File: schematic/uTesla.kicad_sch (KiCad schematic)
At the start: 0 parts

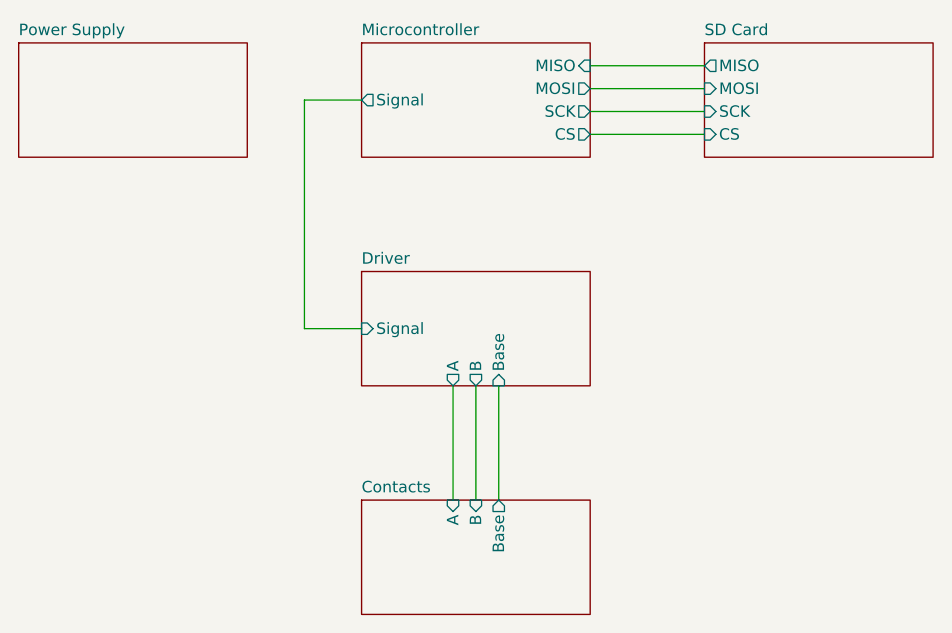
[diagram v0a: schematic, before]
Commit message: Create SD card schematic
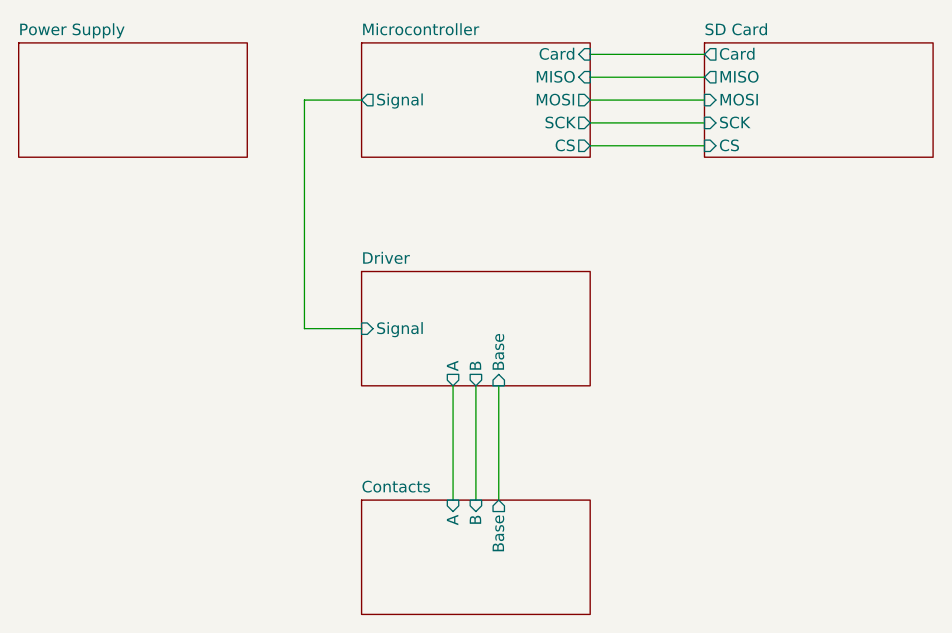
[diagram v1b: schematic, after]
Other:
- sheet Microcontroller ports: added Card; removed none
- sheet SD Card ports: added Card; removed none
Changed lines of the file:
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@@
 (kicad_sch (version 20230121) (generator eeschema)
   (paper "A4")
-  (wire (pts (xy 152.4 71.12) (xy 165.1 71.12))
-    (stroke (width 0) (type default))
-  )
   (wire (pts (xy 139.7 101.6) (xy 139.7 114.3))
     (stroke (width 0) (type default))
   )
-  (wire (pts (xy 152.4 73.66) (xy 165.1 73.66))
-    (stroke (width 0) (type default))
-  )
-  (wire (pts (xy 152.4 68.58) (xy 165.1 68.58))
-    (stroke (width 0) (type default))
-  )
-  (wire (pts (xy 152.4 66.04) (xy 165.1 66.04))
+  (wire (pts (xy 152.4 67.31) (xy 165.1 67.31))
     (stroke (width 0) (type default))
   )
@@
   )
   (wire (pts (xy 127 69.85) (xy 120.65 69.85))
+    (stroke (width 0) (type default))
+  )
+  (wire (pts (xy 152.4 64.77) (xy 165.1 64.77))
     (stroke (width 0) (type default))
   )
@@
   )
   (wire (pts (xy 142.24 101.6) (xy 142.24 114.3))
+    (stroke (width 0) (type default))
+  )
+  (wire (pts (xy 152.4 72.39) (xy 165.1 72.39))
+    (stroke (width 0) (type default))
+  )
+  (wire (pts (xy 152.4 74.93) (xy 165.1 74.93))
+    (stroke (width 0) (type default))
+  )
+  (wire (pts (xy 152.4 69.85) (xy 165.1 69.85))
     (stroke (width 0) (type default))
   )
@@
     (instances
       (project "uTesla"
-        (path "/0cecab2b-a552-4f9c-b012-66fc2b7d8bdb" (page "4"))
+        (path "/0cecab2b-a552-4f9c-b012-66fc2b7d8bdb" (page "5"))
       )
     )
@@
       (effects (font (size 1.27 1.27)) (justify left top) hide)
     )
-    (pin "MISO" output (at 165.1 66.04 180)
+    (pin "MISO" output (at 165.1 67.31 180)
       (effects (font (size 1.27 1.27)) (justify left))
     )
-    (pin "SCK" input (at 165.1 71.12 180)
+    (pin "SCK" input (at 165.1 72.39 180)
       (effects (font (size 1.27 1.27)) (justify left))
     )
-    (pin "CS" input (at 165.1 73.66 180)
+    (pin "CS" input (at 165.1 74.93 180)
       (effects (font (size 1.27 1.27)) (justify left))
     )
-    (pin "MOSI" input (at 165.1 68.58 180)
+    (pin "MOSI" input (at 165.1 69.85 180)
+      (effects (font (size 1.27 1.27)) (justify left))
+    )
+    (pin "Card" output (at 165.1 64.77 180)
       (effects (font (size 1.27 1.27)) (justify left))
     )
     (instances
       (project "uTesla"
-        (path "/0cecab2b-a552-4f9c-b012-66fc2b7d8bdb" (page "5"))
+        (path "/0cecab2b-a552-4f9c-b012-66fc2b7d8bdb" (page "4"))
       )
     )
@@
       (effects (font (size 1.27 1.27)) (justify left))
     )
-    (pin "MOSI" output (at 152.4 68.58 0)
+    (pin "MOSI" output (at 152.4 69.85 0)
       (effects (font (size 1.27 1.27)) (justify right))
     )
-    (pin "CS" output (at 152.4 73.66 0)
+    (pin "CS" output (at 152.4 74.93 0)
       (effects (font (size 1.27 1.27)) (justify right))
     )
-    (pin "MISO" input (at 152.4 66.04 0)
+    (pin "MISO" input (at 152.4 67.31 0)
       (effects (font (size 1.27 1.27)) (justify right))
     )
-    (pin "SCK" output (at 152.4 71.12 0)
+    (pin "SCK" output (at 152.4 72.39 0)
       (effects (font (size 1.27 1.27)) (justify right))
     )
+    (pin "Card" input (at 152.4 64.77 0)
+      (effects (font (size 1.27 1.27)) (justify right))
+    )

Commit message: Create driver schematic
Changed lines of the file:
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@@
       (effects (font (size 1.27 1.27)) (justify left top) hide)
     )
-    (pin "A" input (at 137.16 114.3 90)
+    (pin "Base" output (at 142.24 114.3 90)
       (effects (font (size 1.27 1.27)) (justify right))
     )
-    (pin "B" input (at 139.7 114.3 90)
+    (pin "A" output (at 137.16 114.3 90)
       (effects (font (size 1.27 1.27)) (justify right))
     )
-    (pin "Base" output (at 142.24 114.3 90)
+    (pin "B" output (at 139.7 114.3 90)
       (effects (font (size 1.27 1.27)) (justify right))
     )
@@
       (effects (font (size 1.27 1.27)) (justify left))
     )
-    (pin "A" output (at 137.16 101.6 270)
-      (effects (font (size 1.27 1.27)) (justify left))
-    )
-    (pin "B" output (at 139.7 101.6 270)
-      (effects (font (size 1.27 1.27)) (justify left))
-    )
     (pin "Base" input (at 142.24 101.6 270)
       (effects (font (size 1.27 1.27)) (justify left))
     )
+    (pin "A" input (at 137.16 101.6 270)
+      (effects (font (size 1.27 1.27)) (justify left))
+    )
+    (pin "B" input (at 139.7 101.6 270)
+      (effects (font (size 1.27 1.27)) (justify left))
+    )
